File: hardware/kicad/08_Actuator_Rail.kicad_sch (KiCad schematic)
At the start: 16 parts

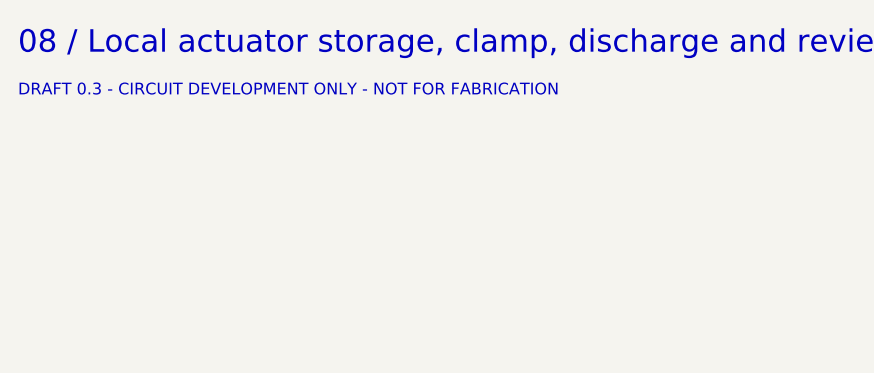
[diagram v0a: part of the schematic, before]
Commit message: Allocate ESP32-S3 GPIO and peripheral resources
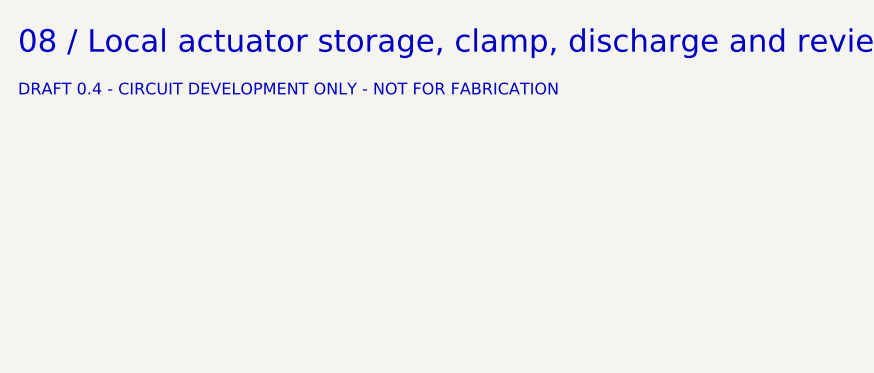
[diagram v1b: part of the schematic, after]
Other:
- note added: "DRAFT 0.4 - CIRCUIT DEVELOPMENT ONLY - NOT FOR FABRICATION"
- note removed: "DRAFT 0.3 - CIRCUIT DEVELOPMENT ONLY - NOT FOR FABRICATION"
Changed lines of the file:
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@@
     (title "MagMouse - 08_Actuator_Rail")
     (date "2026-09-08")
-    (rev "0.3 DRAFT")
+    (rev "0.4 DRAFT")
     (company "MagMouse")
     (comment 1 "NOT FOR FABRICATION - unresolved circuits listed in README.md"))
@@
       (justify left top))
 )
-  (text "DRAFT 0.3 - CIRCUIT DEVELOPMENT ONLY - NOT FOR FABRICATION"
+  (text "DRAFT 0.4 - CIRCUIT DEVELOPMENT ONLY - NOT FOR FABRICATION"
     (at 20 24 0)
     (effects
